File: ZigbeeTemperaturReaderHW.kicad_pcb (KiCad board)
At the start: 2 copper layers, 0 parts

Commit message: schema and placed
Draw full schematic (ESP32-C6-Zero, OLED, DS18B20 jack connectors,
LDO regulator, battery holder, pairing button, I2C pull-ups) and wire
all nets with global labels and power symbols. Add footprint library
table entries and component reference documentation.

Co-Authored-By: Claude Sonnet 5 <noreply@anthropic.com>
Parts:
- added BAT2: ~, Mechanical:BatteryHolder_3xAAA, B.Cu at (0.00, -0.29)
- added C1: CC1206KRX7R9BB104, Passive:C_1206_3216Metric, F.Cu at (-14.0, -30.5)
- added C2: CC1206KRX7R9BB104, Passive:C_1206_3216Metric, F.Cu at (-14.0, -17.8)
- added C4: CC1206KRX7R9BB104, Passive:C_1206_3216Metric, F.Cu at (-7.00, -7.50)
- added C5: CC1206KRX7R9BB104, Passive:C_1206_3216Metric, F.Cu at (0.00, 27.0)
- added C6: CC1206KKX7RDBB102, Passive:C_1206_3216Metric, F.Cu at (-14.0, -8.89)
- added JP1: ~, Connectors:JY039-5P, F.Cu at (-10.0, 28.0)
- added JP2: ~, Connectors:JY039-5P, F.Cu at (10.0, 28.0)
- added OLED2: ~, Modules:OLED-0.96-SSD1306-I2C, F.Cu at (0.00, 11.0)
- added R1: RC1206JR-7W1RLC19632287, Passive:R_1206_3216Metric, F.Cu at (-14.0, -12.7)
- added R2: RC1206JR-7W1RLC19632287, Passive:R_1206_3216Metric, F.Cu at (12.7, -25.4)
- added R3: RC1206JR-7W1RLC19632287, Passive:R_1206_3216Metric, F.Cu at (12.7, -22.9)
- added R4: RC1206JR-7W1RLC19632287, Passive:R_1206_3216Metric, F.Cu at (7.00, -7.50)
- added S2: TL1105BF160Q, Mechanical:SW_TL1105BF160Q, F.Cu at (0.00, -7.50)
- added U1: ~, Modules:Waveshare-ESP32-C6-Zero, F.Cu at (0.00, -25.4)
- added U2: RT9080-33GJ5, Power:TSOT-23-5_RIT-L, F.Cu at (-14.0, -22.9)
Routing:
- net VCC3V3: track 0.00 -> 3.00 mm
- net GND: vias 0 -> 1
- net (no net): vias 0 -> 5
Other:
- board outline added: 48 x 74 mm

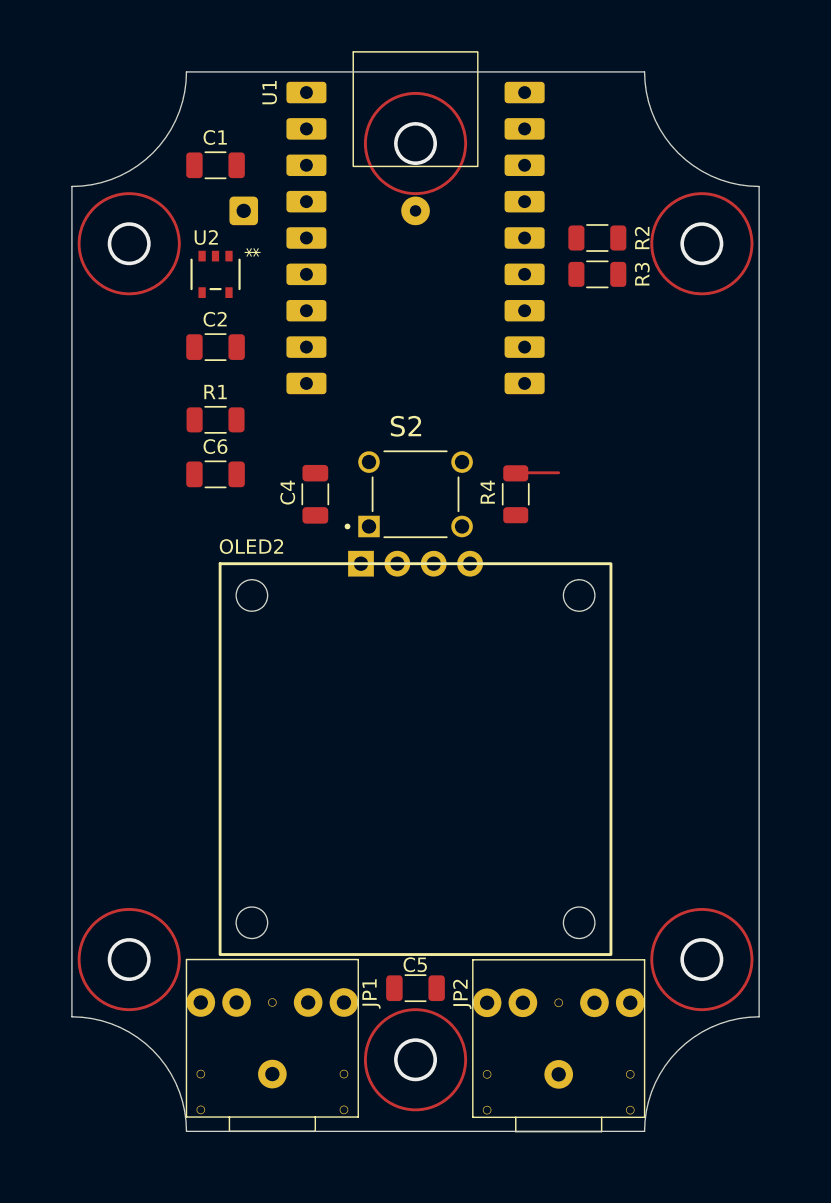
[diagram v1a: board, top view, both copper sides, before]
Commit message: Add VCC3V3/GND copper pours and route remaining nets
- VCC3V3 filled zone on F.Cu, GND filled zone on B.Cu, clipped to the
  board outline and the ESP32-C6 antenna keepout
- Route all remaining signal nets (OLED_SCL/SDA, ONE_WIRE, PAIRING,
  SENSOR_POWER, Net-BAT2-VCC4V5) with vertical tracks on F.Cu and
  horizontal tracks on B.Cu, connected by vias
- Stitch SMD-only GND pads to the bottom GND pour with a short via
  at each pad

Co-Authored-By: Claude Sonnet 5 <noreply@anthropic.com>
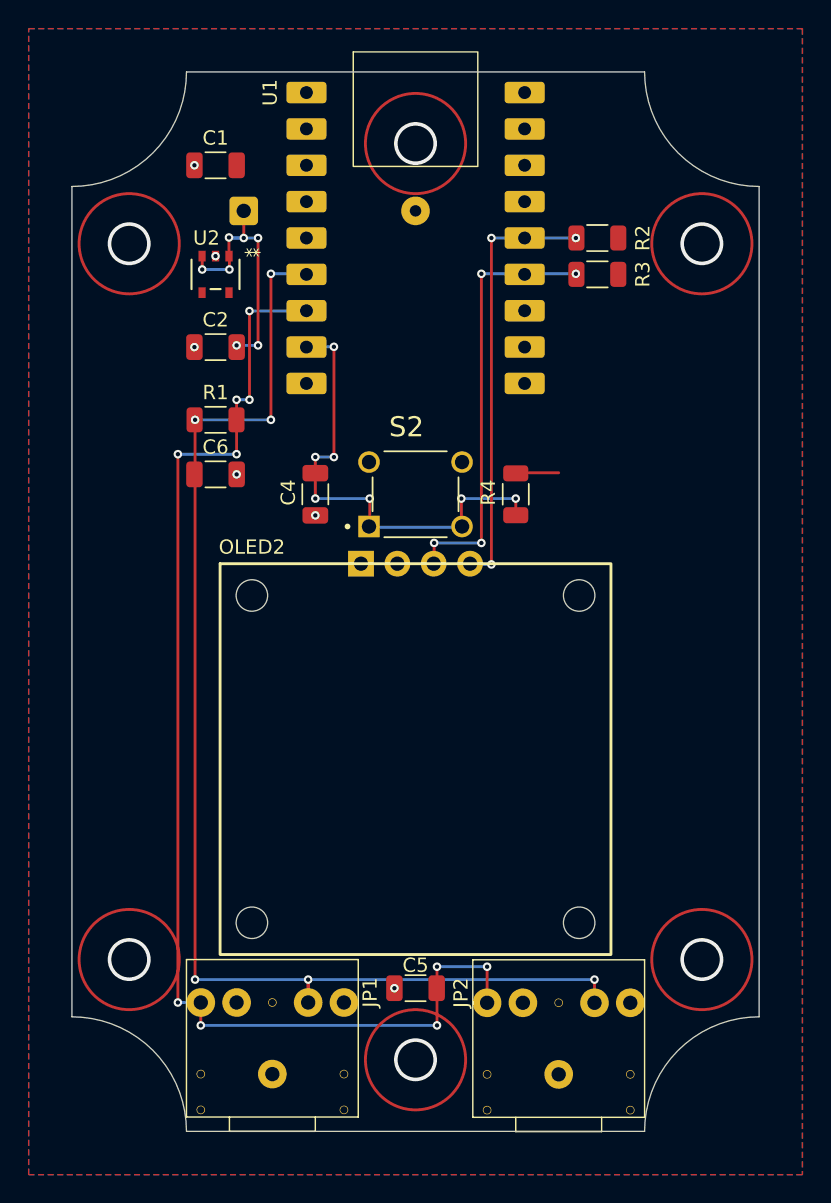
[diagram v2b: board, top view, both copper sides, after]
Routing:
- net ONE_WIRE: track 0.00 -> 89.8 mm, vias 0 -> 6
- net SENSOR_POWER: track 0.00 -> 87.1 mm, vias 0 -> 10
- net PAIRING: track 0.00 -> 33.0 mm, vias 0 -> 7
- net OLED_SDA: track 0.00 -> 30.2 mm, vias 0 -> 3
- net OLED_SCL: track 0.00 -> 30.2 mm, vias 0 -> 4
- net Net-(BAT2-VCC4V5): track 0.00 -> 19.0 mm, vias 0 -> 7
- net GND: vias 1 -> 7
- added copper zone on B.Cu, net GND
- added copper zone on F.Cu, net VCC3V3

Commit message: Add board dimensions and JLCPCB Gerber/drill export
- Add overall width/height dimension annotations (48.00 x 74.00 mm)
  on the Dwgs.User layer
- Include schematic edits made in the KiCad session
- Add Gerber and Excellon drill files for JLCPCB ordering, plus a
  ready-to-upload ZIP archive

Co-Authored-By: Claude Sonnet 5 <noreply@anthropic.com>
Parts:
- JP1, JP2: value ~ -> FC68133
- moved BAT2 184.9 mm to (157.8, 96.2)
- moved C1 184.9 mm to (143.8, 66.0)
- moved C2 184.9 mm to (143.8, 78.7)
- moved C4 184.9 mm to (150.8, 89.0)
- moved C5 184.9 mm to (157.8, 123.5)
- moved C6 184.9 mm to (143.8, 87.6)
- moved JP1 184.9 mm to (147.8, 124.5)
- moved JP2 184.9 mm to (167.8, 124.5)
- moved OLED2 184.9 mm to (157.8, 107.5)
- moved R1 184.9 mm to (143.8, 83.8)
- moved R2 184.9 mm to (170.5, 71.1)
- moved R3 184.9 mm to (170.5, 73.6)
- moved R4 184.9 mm to (164.8, 89.0)
- moved S2 184.9 mm to (157.8, 89.0)
- moved U1 184.9 mm to (157.8, 71.1)
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
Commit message: Add nameplate silkscreen text on bottom layer
TemperaturReader V1.0 (c) by JoWizard 13.09.2026, placed in the open
area next to the battery holder outline on B.SilkS.

Co-Authored-By: Claude Sonnet 5 <noreply@anthropic.com>
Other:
- board text added: "(c) by JoWizard 13.09.2026"
- board text added: "TemperaturReader V1.0"
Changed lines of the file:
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@@
 		(layer "Edge.Cuts")
+	)
+	(gr_text "(c) by JoWizard 13.09.2026"
+		(at 179.07 97.79 90)
+		(layer "B.SilkS")
+		(effects
+			(font
+				(size 1.5 1.5)
+				(thickness 0.3)
+			)
+			(justify mirror)
+		)
+	)
+	(gr_text "TemperaturReader V1.0"
+		(at 175.895 99.695 90)
+		(layer "B.SilkS")
+		(effects
+			(font
+				(size 1.5 1.5)
+				(thickness 0.3)
+				(bold yes)
+			)
+			(justify mirror)
+		)
 	)
 	(dimension
